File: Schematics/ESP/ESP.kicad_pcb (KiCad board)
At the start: 2 copper layers, 180.5 x 111.7 mm, 82 parts, among them J1 Barrel_Jack, J11 Bumper 1, J12 Bumper 2, J13 Battery Input, J14 Conn_02x19_Odd_Even, J15 UltraSconic B, J16 Conn_02x19_Odd_Even, J2 IMU, J3 Battery charger, J4 Motor A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

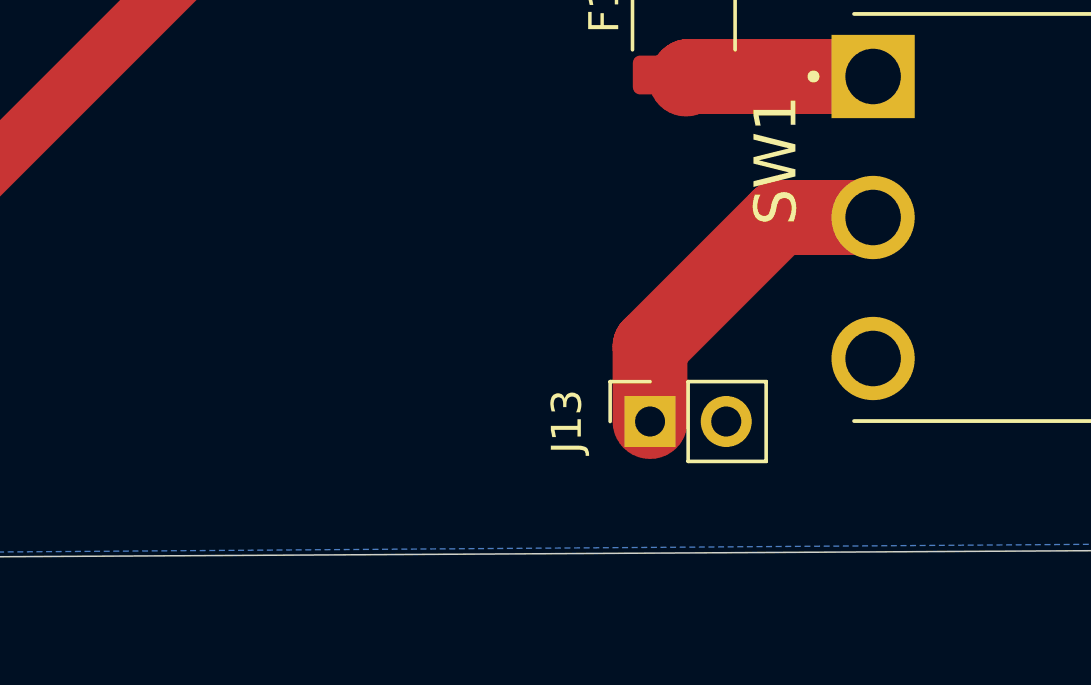
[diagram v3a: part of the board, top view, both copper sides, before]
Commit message: Added footprints for battery input and battery charger with BOM updates
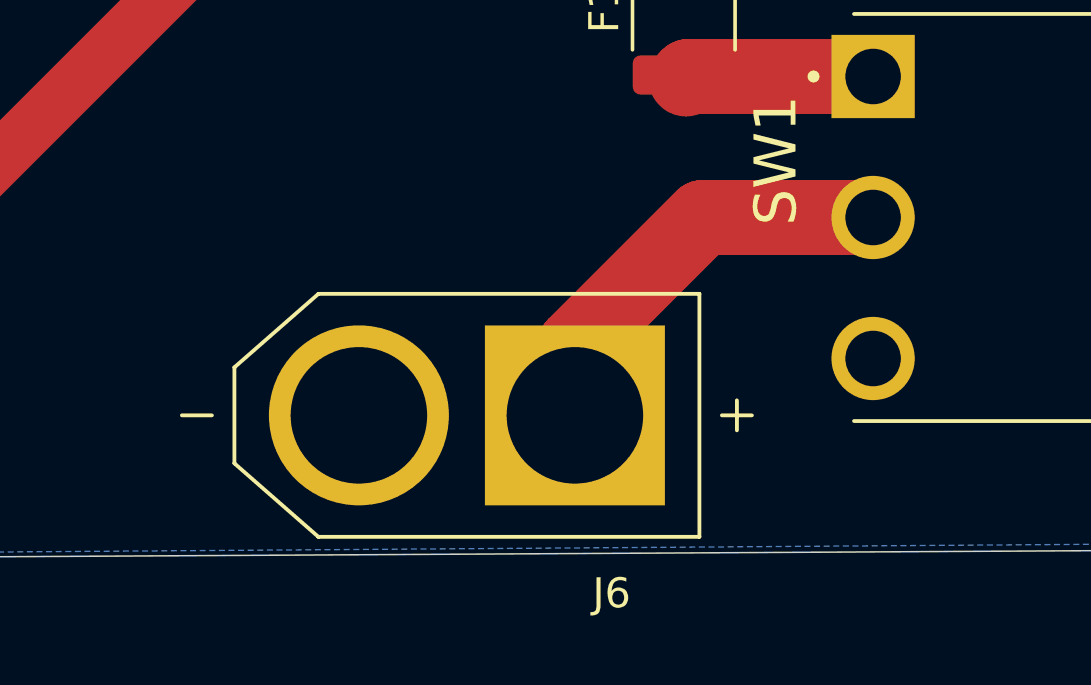
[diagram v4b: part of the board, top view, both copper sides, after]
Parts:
- removed J13: Battery Input, Connector_PinSocket_2.54mm:PinSocket_1x02_P2.54mm_Vertical
- added J6: XT60-M, 500SSP1S1M6QEA:AMASS_XT60-M, F.Cu at (141.0, 166.4)
- R2, R5, R6, R9: value 1k -> 100
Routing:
- net Battery+: track 11.7 -> 14.0 mm
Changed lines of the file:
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@@
     )
   )
-  (footprint "Connector_PinSocket_2.54mm:PinSocket_1x02_P2.54mm_Vertical" (layer "F.Cu")
-    (at 147.075 166.575 90)
-    (descr "Through hole straight socket strip, 1x02, 2.54mm pitch, single row (from Kicad 4.0.7), script generated")
-    (tags "Through hole socket strip THT 1x02 2.54mm single row")
-    (property "Sheetfile" "Peripherals.kicad_sch")
-    (property "Sheetname" "Peripherals")
-    (property "digikey link" "https://www.digikey.com/en/products/detail/sullins-connector-solutions/PPTC021LFBN-RC/810142")
-    (property "ki_description" "Generic connector, single row, 01x02, script generated")
-    (property "ki_keywords" "connector")
-    (attr through_hole)
-    (fp_text reference "J13" (at 0 -2.77 90) (layer "F.SilkS")
-        (effects (font (size 1 1) (thickness 0.15)))
-    )
-    (fp_text value "Battery Input" (at -3.125 0.725 180) (layer "F.Fab")
-        (effects (font (size 1 1) (thickness 0.15)))
-    )
-    (fp_text user "${REFERENCE}" (at 0 1.27) (layer "F.Fab")
-        (effects (font (size 1 1) (thickness 0.15)))
-    )
-    (fp_line (start -1.33 1.27) (end -1.33 3.87)
-      (stroke (width 0.12) (type solid)) (layer "F.SilkS"))
-    (fp_line (start -1.33 1.27) (end 1.33 1.27)
-      (stroke (width 0.12) (type solid)) (layer "F.SilkS"))
-    (fp_line (start -1.33 3.87) (end 1.33 3.87)
-      (stroke (width 0.12) (type solid)) (layer "F.SilkS"))
-    (fp_line (start 0 -1.33) (end 1.33 -1.33)
-      (stroke (width 0.12) (type solid)) (layer "F.SilkS"))
-    (fp_line (start 1.33 -1.33) (end 1.33 0)
-      (stroke (width 0.12) (type solid)) (layer "F.SilkS"))
-    (fp_line (start 1.33 1.27) (end 1.33 3.87)
-      (stroke (width 0.12) (type solid)) (layer "F.SilkS"))
-    (fp_line (start -1.8 -1.8) (end 1.75 -1.8)
-      (stroke (width 0.05) (type solid)) (layer "F.CrtYd"))
-    (fp_line (start -1.8 4.3) (end -1.8 -1.8)
-      (stroke (width 0.05) (type solid)) (layer "F.CrtYd"))
-    (fp_line (start 1.75 -1.8) (end 1.75 4.3)
-      (stroke (width 0.05) (type solid)) (layer "F.CrtYd"))
-    (fp_line (start 1.75 4.3) (end -1.8 4.3)
-      (stroke (width 0.05) (type solid)) (layer "F.CrtYd"))
-    (fp_line (start -1.27 -1.27) (end 0.635 -1.27)
-      (stroke (width 0.1) (type solid)) (layer "F.Fab"))
-    (fp_line (start -1.27 3.81) (end -1.27 -1.27)
-      (stroke (width 0.1) (type solid)) (layer "F.Fab"))
-    (fp_line (start 0.635 -1.27) (end 1.27 -0.635)
-      (stroke (width 0.1) (type solid)) (layer "F.Fab"))
-    (fp_line (start 1.27 -0.635) (end 1.27 3.81)
-      (stroke (width 0.1) (type solid)) (layer "F.Fab"))
-    (fp_line (start 1.27 3.81) (end -1.27 3.81)
-      (stroke (width 0.1) (type solid)) (layer "F.Fab"))
-    (pad "1" thru_hole rect (at 0 0 90) (size 1.7 1.7) (drill 1) (layers "*.Cu" "*.Mask")
-      (net 8 "Battery+") (pinfunction "Pin_1") (pintype "passive"))
-    (pad "2" thru_hole oval (at 0 2.54 90) (size 1.7 1.7) (drill 1) (layers "*.Cu" "*.Mask")
-      (net 1 "Battery-") (pinfunction "Pin_2") (pintype "passive"))
-    (model "${KICAD6_3DMODEL_DIR}/Connector_PinSocket_2.54mm.3dshapes/PinSocket_1x02_P2.54mm_Vertical.wrl"
-      (offset (xyz 0 0 0))
-      (scale (xyz 1 1 1))
-      (rotate (xyz 0 0 0))
-    )
-  )
   (footprint "Package_TO_SOT_SMD:TO-263-5_TabPin3" (layer "F.Cu")
     (at 152.425 123.625 180)
@@
     )
   )
+  (footprint "500SSP1S1M6QEA:AMASS_XT60-M" (layer "F.Cu")
+    (at 140.97 166.37 180)
+    (property "MANUFACTURER" "AMASS")
+    (property "MAXIMUM_PACKAGE_HEIGHT" "16.00 mm")
+    (property "PARTREV" "V1.2")
+    (property "STANDARD" "IPC 7351B")
+    (property "Sheetfile" "Peripherals.kicad_sch")
+    (property "Sheetname" "Peripherals")
+    (attr through_hole)
+    (fp_text reference "J6" (at -4.825 -5.935) (layer "F.SilkS")
+        (effects (font (size 1 1) (thickness 0.15)))
+    )
+    (fp_text value "XT60-M" (at -0.38 5.935) (layer "F.Fab")
+        (effects (font (size 1 1) (thickness 0.15)))
+    )
+    (fp_line (start -9.5 0) (end -8.5 0)
+      (stroke (width 0.127) (type solid)) (layer "F.SilkS"))
+    (fp_line (start -9 -0.5) (end -9 0.5)
+      (stroke (width 0.127) (type solid)) (layer "F.SilkS"))
+    (fp_line (start -7.75 -4.05) (end 4.95 -4.05)
+      (stroke (width 0.127) (type solid)) (layer "F.SilkS"))
+    (fp_line (start -7.75 4.05) (end -7.75 -4.05)
+      (stroke (width 0.127) (type solid)) (layer "F.SilkS"))
+    (fp_line (start 4.95 -4.05) (end 7.75 -1.6)
+      (stroke (width 0.127) (type solid)) (layer "F.SilkS"))
+    (fp_line (start 4.95 4.05) (end -7.75 4.05)
+      (stroke (width 0.127) (type solid)) (layer "F.SilkS"))
+    (fp_line (start 7.75 -1.6) (end 7.75 1.6)
+      (stroke (width 0.127) (type solid)) (layer "F.SilkS"))
+    (fp_line (start 7.75 1.6) (end 4.95 4.05)
+      (stroke (width 0.127) (type solid)) (layer "F.SilkS"))
+    (fp_line (start 8.5 0) (end 9.5 0)
+      (stroke (width 0.127) (type solid)) (layer "F.SilkS"))
+    (fp_line (start -8 -4.3) (end -8 4.3)
+      (stroke (width 0.05) (type solid)) (layer "F.CrtYd"))
+    (fp_line (start -8 4.3) (end 8 4.3)
+      (stroke (width 0.05) (type solid)) (layer "F.CrtYd"))
+    (fp_line (start 8 -4.3) (end -8 -4.3)
+      (stroke (width 0.05) (type solid)) (layer "F.CrtYd"))
+    (fp_line (start 8 4.3) (end 8 -4.3)
+      (stroke (width 0.05) (type solid)) (layer "F.CrtYd"))
+    (fp_line (start -9.5 0) (end -8.5 0)
+      (stroke (width 0.127) (type solid)) (layer "F.Fab"))
+    (fp_line (start -9 -0.5) (end -9 0.5)
+      (stroke (width 0.127) (type solid)) (layer "F.Fab"))
+    (fp_line (start -7.75 -4.05) (end 4.95 -4.05)
+      (stroke (width 0.127) (type solid)) (layer "F.Fab"))
+    (fp_line (start -7.75 4.05) (end -7.75 -4.05)
+      (stroke (width 0.127) (type solid)) (layer "F.Fab"))
+    (fp_line (start 4.95 -4.05) (end 7.75 -1.6)
+      (stroke (width 0.127) (type solid)) (layer "F.Fab"))
+    (fp_line (start 4.95 4.05) (end -7.75 4.05)
+      (stroke (width 0.127) (type solid)) (layer "F.Fab"))
+    (fp_line (start 7.75 -1.6) (end 7.75 1.6)
+      (stroke (width 0.127) (type solid)) (layer "F.Fab"))
+    (fp_line (start 7.75 1.6) (end 4.95 4.05)
+      (stroke (width 0.127) (type solid)) (layer "F.Fab"))
+    (fp_line (start 8.5 0) (end 9.5 0)
+      (stroke (width 0.127) (type solid)) (layer "F.Fab"))
+    (pad "N" thru_hole circle (at 3.6 0 180) (size 6 6) (drill 4.55) (layers "*.Cu" "*.Mask")
+      (net 1 "Battery-") (pinfunction "NEG") (pintype "passive"))
+    (pad "P" thru_hole rect (at -3.6 0 180) (size 6 6) (drill 4.55) (layers "*.Cu" "*.Mask")
+      (net 8 "Battery+") (pinfunction "POS") (pintype "passive"))
+  )
   (footprint "Resistor_SMD:R_1206_3216Metric_Pad1.30x1.75mm_HandSolder" placed (layer "F.Cu")
     (at 89.15 149.6 180)
@@
         (effects (font (size 1 1) (thickness 0.15)))
     )
-    (fp_text value "1k" (at 0 1.82 90) (layer "F.Fab")
+    (fp_text value "100" (at 0 1.82 90) (layer "F.Fab")
         (effects (font (size 1 1) (thickness 0.15)))
     )
@@
         (effects (font (size 1 1) (thickness 0.15)))
     )
-    (fp_text value "1k" (at 0 1.82 90) (layer "F.Fab")
+    (fp_text value "100" (at 0 1.82 90) (layer "F.Fab")
         (effects (font (size 1 1) (thickness 0.15)))
     )
@@
         (effects (font (size 1 1) (thickness 0.15)))
     )
-    (fp_text value "1k" (at 0 1.82 90) (layer "F.Fab")
+    (fp_text value "100" (at 0 1.82 90) (layer "F.Fab")
         (effects (font (size 1 1) (thickness 0.15)))
     )
@@
         (effects (font (size 1 1) (thickness 0.15)))
     )
-    (fp_text value "1k" (at 0.1 1.82 90) (layer "F.Fab")
+    (fp_text value "100" (at 0.1 1.82 90) (layer "F.Fab")
         (effects (font (size 1 1) (thickness 0.15)))
     )
@@
   (segment (start 80.26 136.2) (end 80.26 129.81) (width 0.3) (layer "F.Cu") (net 6))
   (segment (start 198.92 117.051766) (end 198.92 112.5) (width 0.3) (layer "F.Cu") (net 7))
-  (segment (start 147.075 164.075) (end 151.375 159.775) (width 2.5) (layer "F.Cu") (net 8))
-  (segment (start 147.075 166.575) (end 147.075 164.075) (width 2.5) (layer "F.Cu") (net 8))
-  (segment (start 151.375 159.775) (end 154.51 159.775) (width 2.5) (layer "F.Cu") (net 8))
+  (segment (start 148.835 159.775) (end 154.51 159.775) (width 2.5) (layer "F.Cu") (net 8))
+  (segment (start 144.57 166.37) (end 144.57 164.04) (width 2.5) (layer "F.Cu") (net 8))
+  (segment (start 144.57 164.04) (end 148.835 159.775) (width 2.5) (layer "F.Cu") (net 8))
   (segment (start 201.46 117.16) (end 201.46 112.5) (width 0.3) (layer "F.Cu") (net 9))
   (segment (start 99.4 155.55) (end 102.5 155.55) (width 0.3) (layer "F.Cu") (net 10))

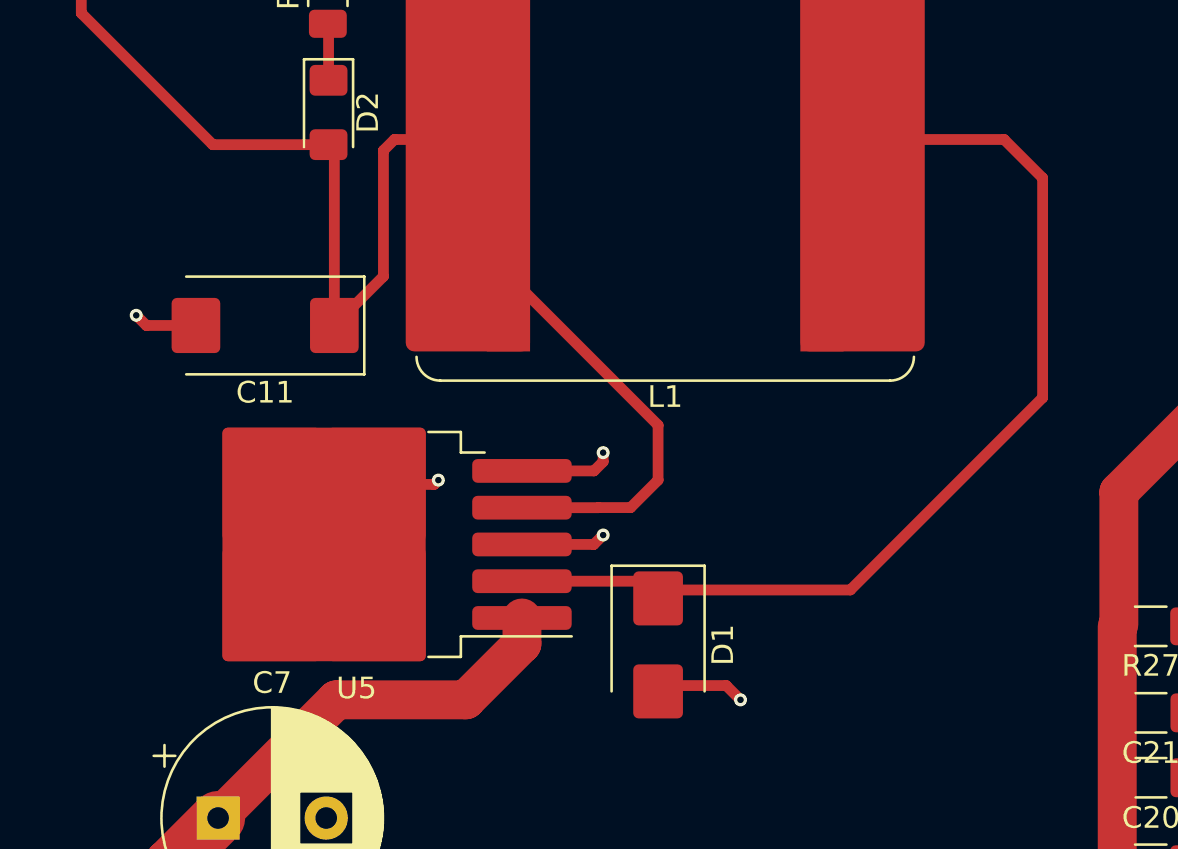
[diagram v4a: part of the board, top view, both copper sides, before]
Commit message: Added footprints for battery input and battery charger with BOM updates
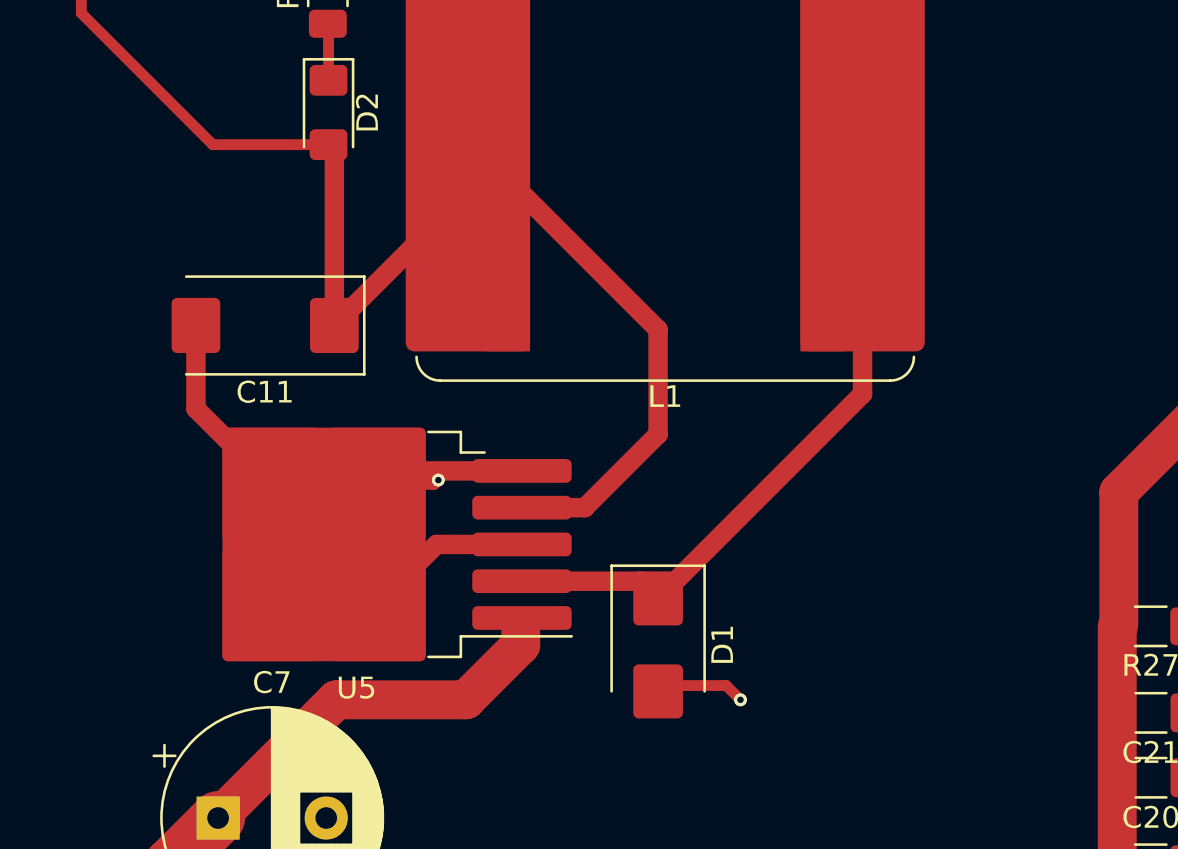
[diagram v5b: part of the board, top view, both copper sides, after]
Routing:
- net Net-(D1-K): track 46.3 -> 31.8 mm
- net Battery-: track 167.8 -> 180.3 mm, vias 22 -> 19
- net +5V: track 183.7 -> 184.9 mm
- net +12V: track 236.3 -> 235.7 mm
